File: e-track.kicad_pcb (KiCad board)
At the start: 2 copper layers, 40 x 40 mm, 35 parts, among them J2 Conn_01x24, J3 Conn_01x06, Q4 BSS138, SW1 SW_Push, SW2 SW_Push, SW3 SW_Push, U1 ESP32-C3-MINI-1, U2 BME280, U5 TPS62842DGR

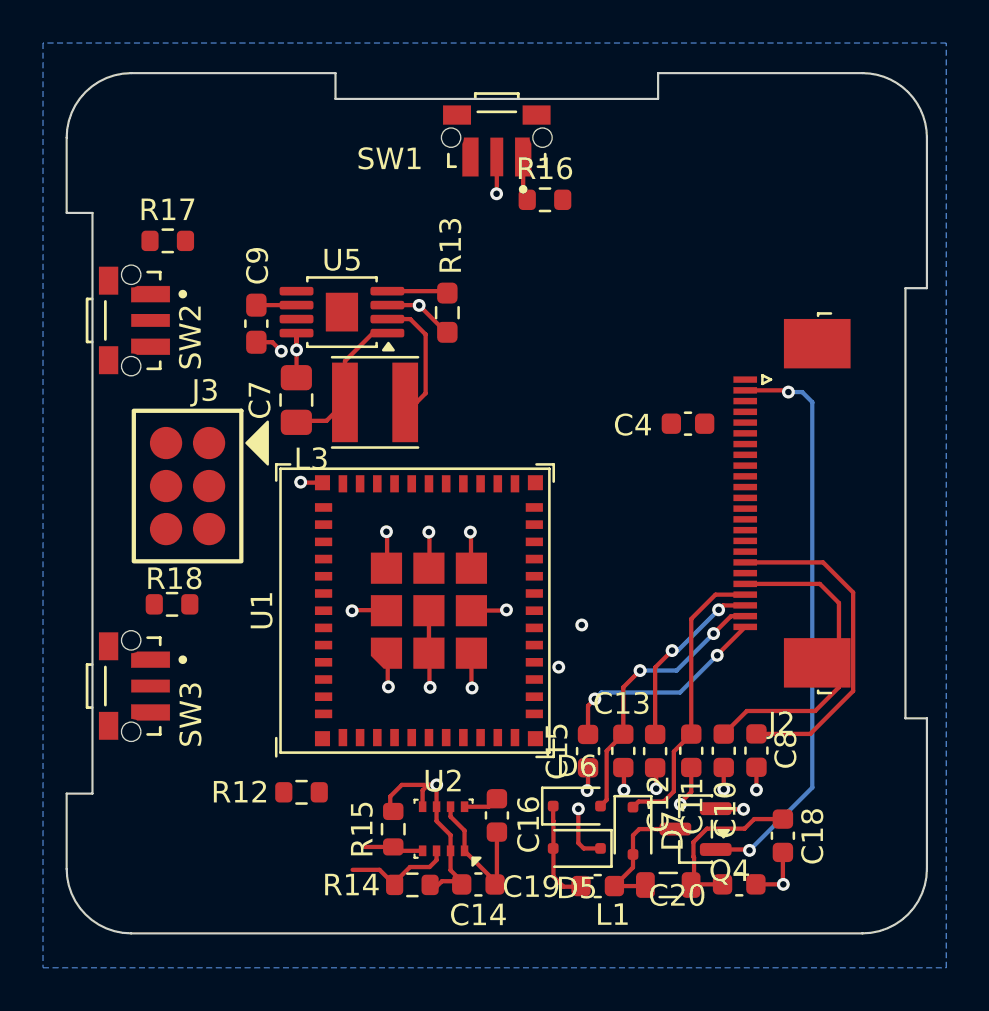
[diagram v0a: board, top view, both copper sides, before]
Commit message: Update PCB design and add SVG exports, improve gitignore
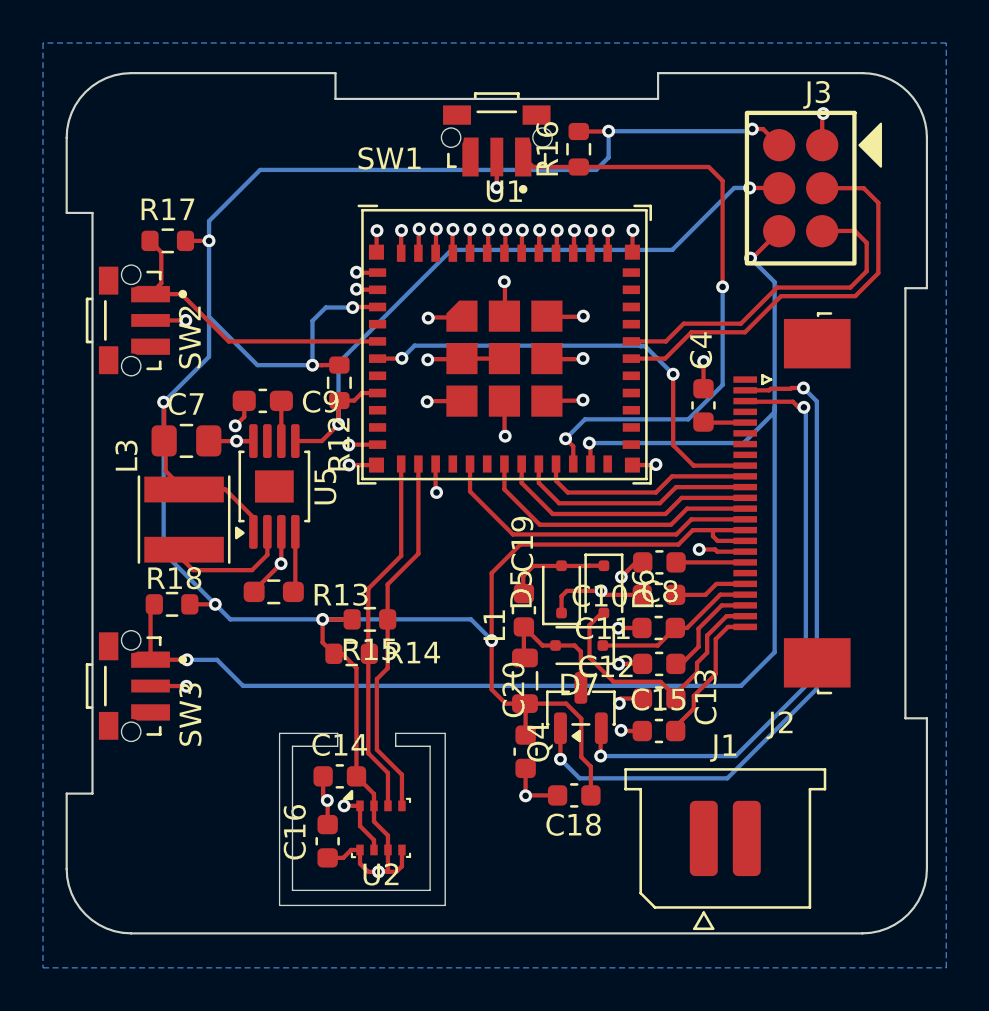
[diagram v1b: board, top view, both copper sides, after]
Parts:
- added J1: Batt, Connector_Samtec_MicroPower:Samtec_UMPS-02-XX.X-X-V-S_1x02_P2.0mm_Socket, F.Cu at (162.7, 111.0)
- J2: value Conn_01x24 -> AFC07-S24ECA-00
- moved J3 31.7 mm to (166.2, 80.8)
- moved R12 19.1 mm to (144.8, 89.8), turned to 90 degrees
- moved R13 15.3 mm to (141.7, 99.5), turned to 180 degrees
- moved C19 13.3 mm to (153.4, 100.4), turned to -90 degrees
- moved U1 13.1 mm to (152.5, 88.0), turned to 0 degrees
- moved D5 12.1 mm to (155.1, 99.4), turned to 90 degrees
- moved C20 11.7 mm to (153.4, 107.0), turned to -90 degrees
- moved L1 11.6 mm to (153.4, 103.7), turned to 90 degrees
- moved R14 11.1 mm to (145.3, 102.4), turned to 180 degrees
- moved L3 10.4 mm to (137.6, 96.2), turned to 90 degrees
- moved D6 10.2 mm to (157.1, 99.4), turned to -90 degrees
- moved C18 9.88 mm to (155.7, 109.0), turned to 0 degrees
- moved C8 9.85 mm to (159.7, 98.2), turned to 0 degrees
- moved R15 9.82 mm to (146.2, 100.8), turned to 180 degrees
- moved D7 8.97 mm to (155.9, 102.0), turned to 180 degrees
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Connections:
- U1 pad 12: /SCL -> /SDA
- U1 pad 13: /SDA -> /SCL
- U1 pad 16: /RST -> /DIN
- U1 pad 18: /DC -> /CLK
- U1 pad 20: /CLK -> /DC
- U1 pad 21: /DIN -> /RST
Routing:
- net +3V3: track 28.4 -> 137.7 mm, vias 1 -> 10
- net /IO: track 0.00 -> 63.9 mm, vias 0 -> 3
- net /EN: track 0.00 -> 32.1 mm, vias 0 -> 2
- net GND: track 44.5 -> 72.5 mm, vias 21 -> 47
- net /MENU: track 2.07 -> 28.9 mm, vias 0 -> 2
- net /e-paper/RESE: track 1.30 -> 28.0 mm, vias 1 -> 2
- net /BUSY: track 0.00 -> 21.6 mm, vias 1 -> 2
- net /RX: track 0.00 -> 19.3 mm
- net /TX: track 0.00 -> 15.9 mm
- net /DIN: track 0.00 -> 15.2 mm
- net /SCL: track 2.80 -> 17.2 mm
- net /UP: track 0.00 -> 14.4 mm
- net /CLK: track 0.00 -> 13.4 mm
- net Net-(J2-Pin_18): track 15.5 -> 3.22 mm
- net /CS: track 0.00 -> 12.2 mm
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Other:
- outline, holes or cut-outs redrawn

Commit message: agregando conector y RTC
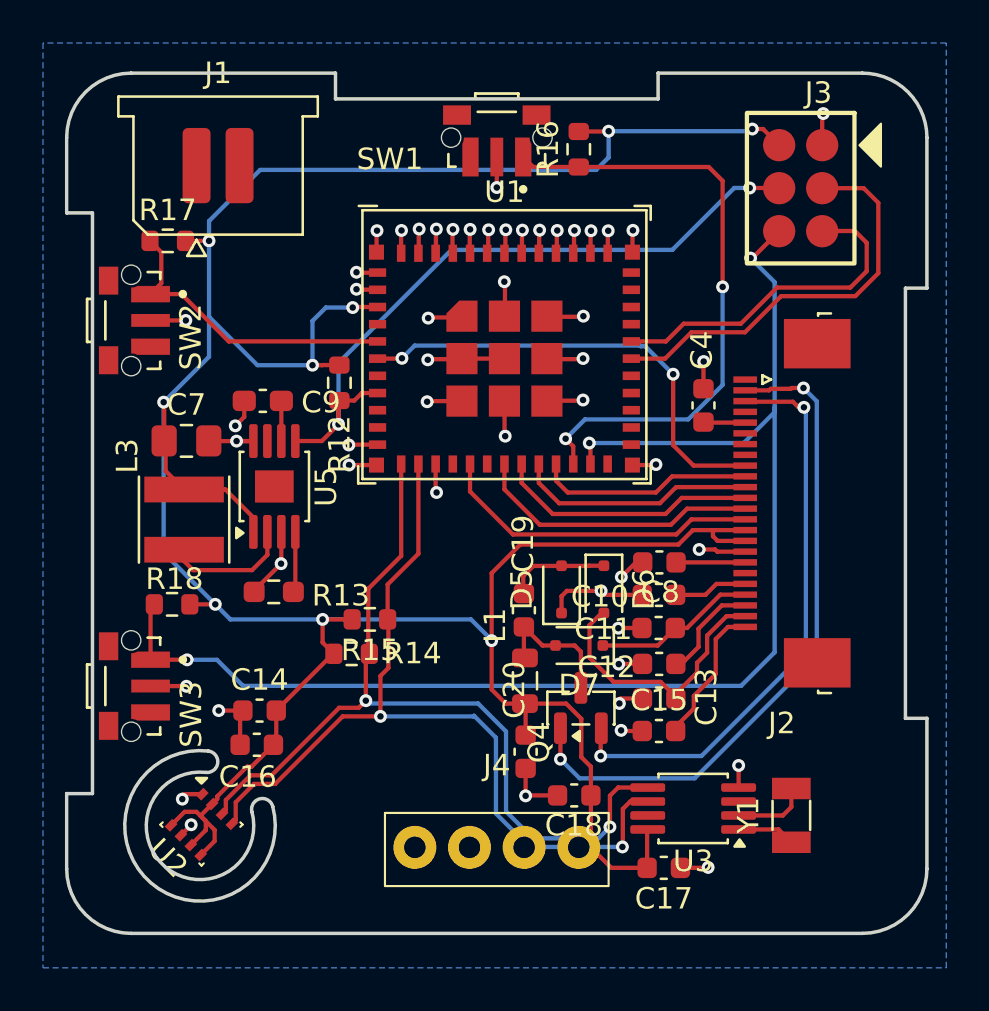
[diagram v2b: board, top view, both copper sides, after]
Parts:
- added C17: 100nF, Capacitor_SMD:C_0603_1608Metric, F.Cu at (159.9, 112.4)
- added J4: Conn_01x04, MR-footprint:pogo-pin-female-4P-2.54, F.Cu at (152.1, 111.4)
- added U3: PCF8563TS, Package_SO:MSOP-8_3x3mm_P0.65mm, F.Cu at (161.2, 109.6)
- added Y1: 32.768kHz, Crystal:Crystal_SMD_3215-2Pin_3.2x1.5mm, F.Cu at (165.8, 109.9)
- moved J1 39.2 mm to (139.1, 79.7)
- moved U2 8.35 mm to (138.4, 110.3), turned to -45 degrees
- moved C16 5.57 mm to (140.9, 106.6), turned to 0 degrees
- moved C14 4.82 mm to (141.1, 105.0)
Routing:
- net /SCL: track 17.2 -> 40.9 mm, vias 0 -> 2
- net /SDA: track 16.9 -> 40.6 mm, vias 0 -> 2
- net +3V3: track 137.7 -> 143.8 mm, vias 10 -> 9
- net Net-(U3-OSCO): track 0.00 -> 3.48 mm
- net Net-(U3-OSCI): track 0.00 -> 2.70 mm
- net GND: track 72.5 -> 74.0 mm, vias 47 -> 50
- net /e-paper/RESE: track 28.0 -> 27.1 mm
- net /e-paper/GDR: track 32.5 -> 31.6 mm
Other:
- outline, holes or cut-outs redrawn
